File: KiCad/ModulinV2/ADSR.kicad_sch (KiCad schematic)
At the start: 54 parts, among them IC34 AS3310D, IC35 AS3310D

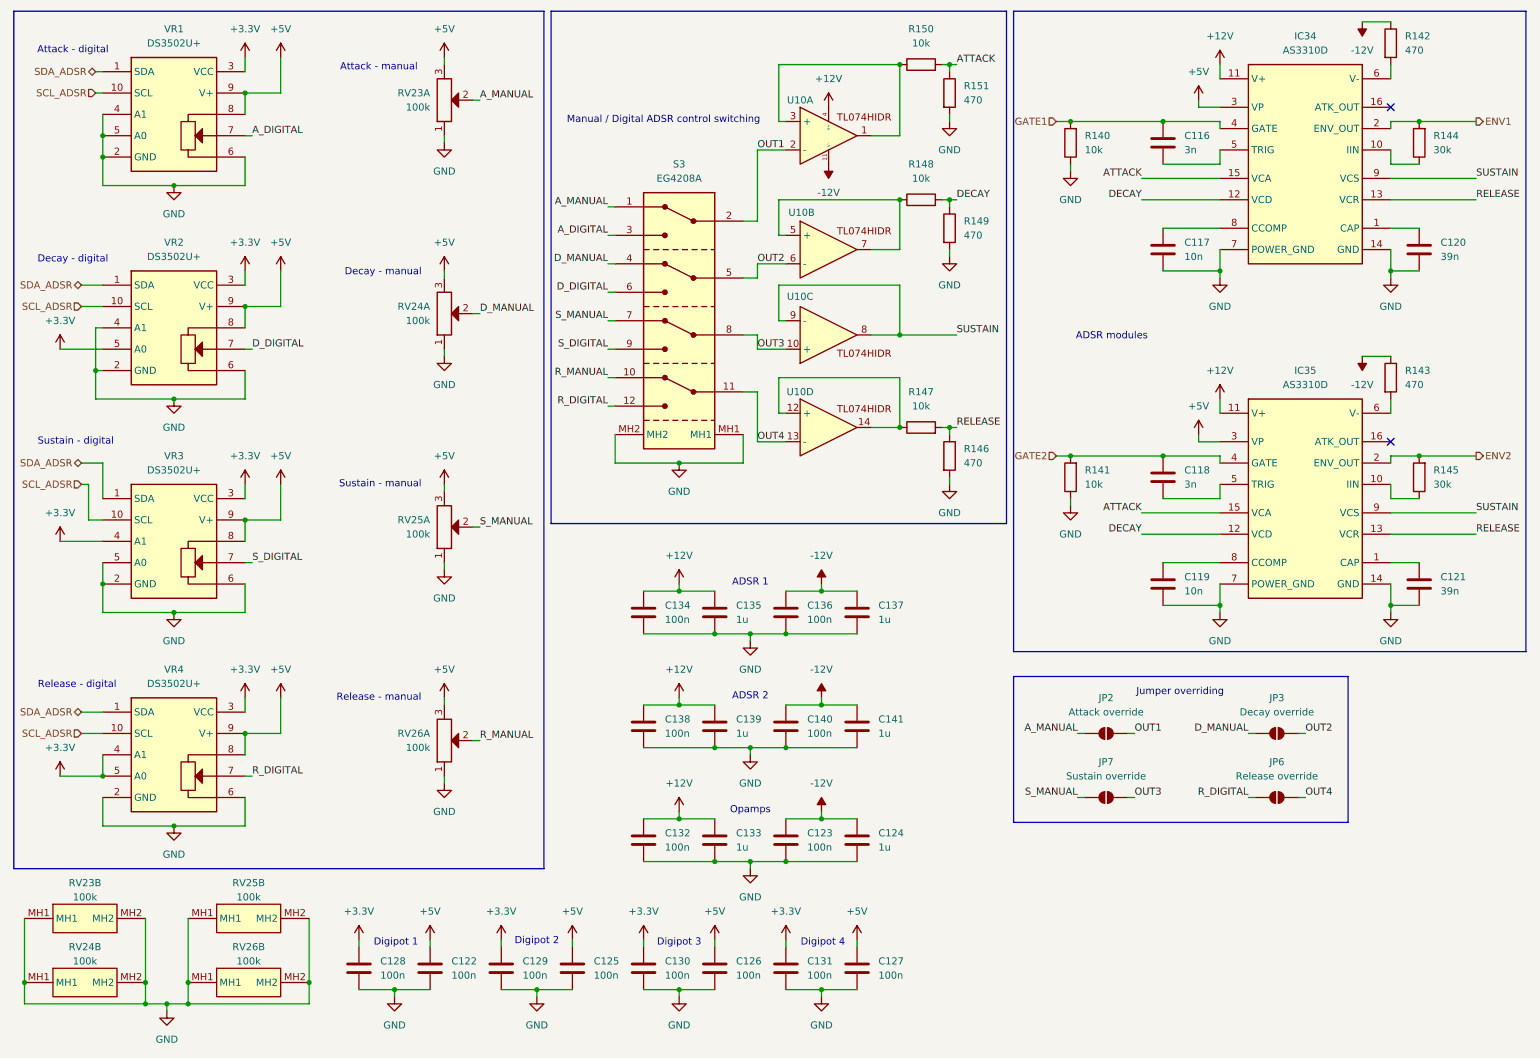
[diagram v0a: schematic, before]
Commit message: Added 4k7 pullups to I2C lines
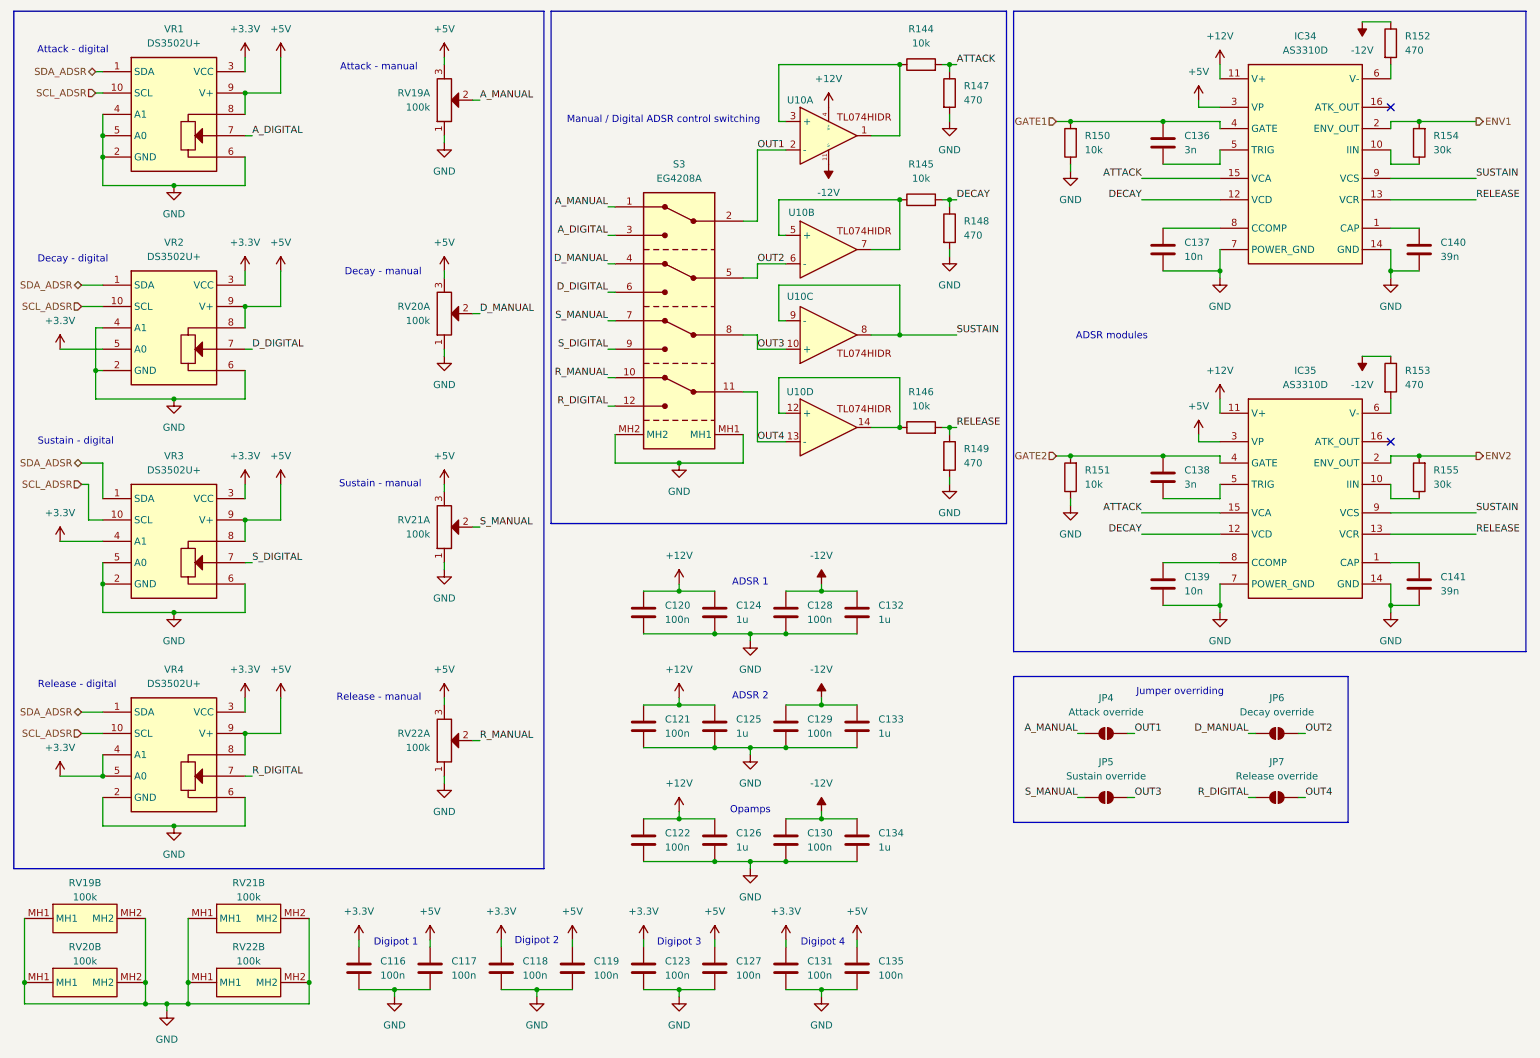
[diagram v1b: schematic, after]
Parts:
- renumbered C128 to C116, C122 to C117, C129 to C118, C125 to C119, C134 to C120, C138 to C121, C132 to C122, C130 to C123, C135 to C124, C139 to C125, C133 to C126, C126 to C127, C136 to C128, C140 to C129, C123 to C130, C137 to C132, C141 to C133, C124 to C134, C127 to C135, C116 to C136, C117 to C137, C118 to C138, C119 to C139, C120 to C140, C121 to C141, JP2 to JP4, JP7 to JP5, JP3 to JP6, JP6 to JP7, R150 to R144, R148 to R145, R147 to R146, R151 to R147, R149 to R148, R146 to R149, R140 to R150, R141 to R151, R142 to R152, R143 to R153, R144 to R154, R145 to R155, RV23 to RV19, RV24 to RV20, RV25 to RV21, RV26 to RV22

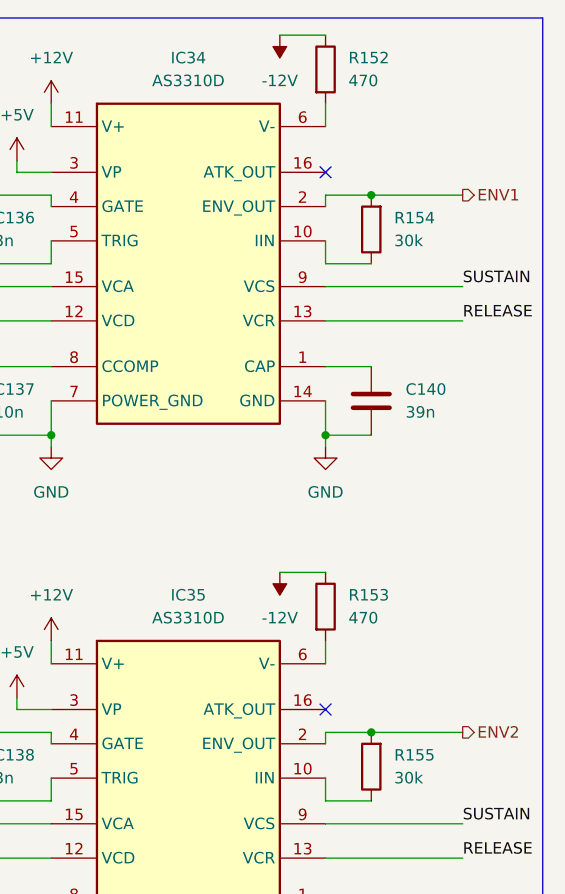
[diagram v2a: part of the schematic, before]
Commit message: Added wave selection jumpers for testing
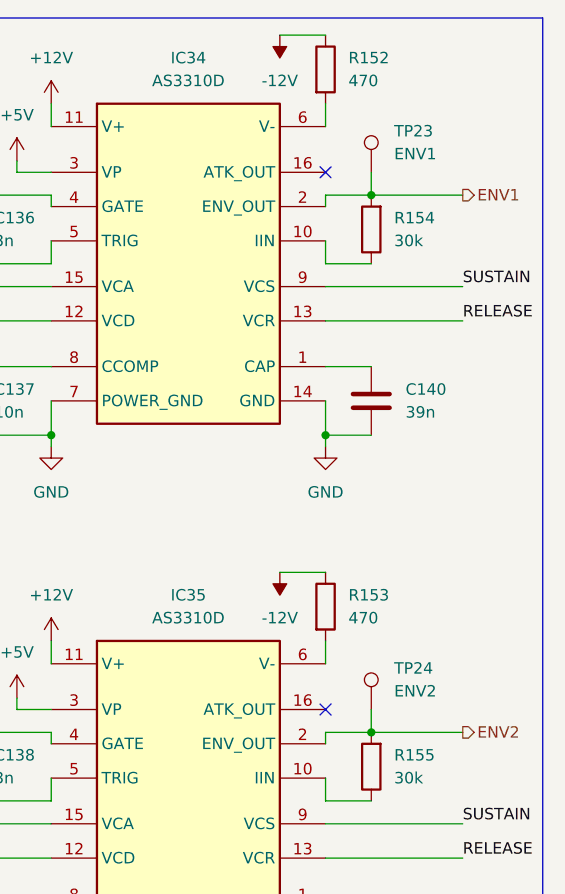
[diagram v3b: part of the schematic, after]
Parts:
- added TP23: ENV1, symbol Connector:TestPoint
- added TP24: ENV2, symbol Connector:TestPoint
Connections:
- net ENV1: now also TP23.1
- net ENV2: now also TP24.1
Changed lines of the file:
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@@
 	(wire
 		(pts
+			(xy 264.16 90.17) (xy 264.16 92.71)
+		)
+		(stroke
+			(width 0)
+			(type default)
+		)
+	)
+	(wire
+		(pts
 			(xy 224.79 29.21) (xy 224.79 30.48)
 		)
@@
 	(wire
 		(pts
+			(xy 264.16 30.48) (xy 264.16 33.02)
+		)
+		(stroke
+			(width 0)
+			(type default)
+		)
+	)
+	(wire
+		(pts
 			(xy 21.59 107.95) (xy 29.21 107.95)
 		)
@@
 	)
 	(symbol
+		(lib_id "Connector:TestPoint")
+		(at 264.16 90.17 0)
+		(unit 1)
+		(exclude_from_sim no)
+		(in_bom yes)
+		(on_board yes)
+		(dnp no)
+		(fields_autoplaced yes)
+		(property "Reference" "TP24"
+			(at 266.7 85.5979 0)
+			(effects
+				(font
+					(size 1.27 1.27)
+				)
+				(justify left)
+			)
+		)
+		(property "Value" "ENV2"
+			(at 266.7 88.1379 0)
+			(effects
+				(font
+					(size 1.27 1.27)
+				)
+				(justify left)
+			)
+		)
+		(property "Footprint" ""
+			(at 269.24 90.17 0)
+			(effects
+				(font
+					(size 1.27 1.27)
+				)
+				(hide yes)
+			)
+		)
+		(property "Datasheet" "~"
+			(at 269.24 90.17 0)
+			(effects
+				(font
+					(size 1.27 1.27)
+				)
+				(hide yes)
+			)
+		)
+		(property "Description" "test point"
+			(at 264.16 90.17 0)
+			(effects
+				(font
+					(size 1.27 1.27)
+				)
+				(hide yes)
+			)
+		)
+		(pin "1"
+		)
+		(instances
+			(project "ModulinV2"
+				(path "/c6b34a57-3941-4b56-8b80-1848c7f41082/72de756e-4613-4cf7-8685-e4594fe0f098"
+					(reference "TP24")
+					(unit 1)
+				)
+			)
+		)
+	)
+	(symbol
 		(lib_id "DS3502U+:DS3502U+")
 		(at 29.21 138.43 0)
@@
 					(unit 1)
 				)
+			)
+		)
+	)
+	(symbol
+		(lib_id "Connector:TestPoint")
+		(at 264.16 30.48 0)
+		(unit 1)
+		(exclude_from_sim no)
+		(in_bom yes)
+		(on_board yes)
+		(dnp no)
+		(fields_autoplaced yes)
+		(property "Reference" "TP23"
+			(at 266.7 25.9079 0)
+			(effects
+				(font
+					(size 1.27 1.27)
+				)
+				(justify left)
+			)
+		)
+		(property "Value" "ENV1"
+			(at 266.7 28.4479 0)
+			(effects
+				(font
+					(size 1.27 1.27)
+				)
+				(justify left)
+			)
+		)
+		(property "Footprint" ""
+			(at 269.24 30.48 0)
+			(effects
+				(font
+					(size 1.27 1.27)
+				)
+				(hide yes)
+			)
+		)
+		(property "Datasheet" "~"
+			(at 269.24 30.48 0)
+			(effects
+				(font
+					(size 1.27 1.27)
+				)
+				(hide yes)
+			)
+		)
+		(property "Description" "test point"
+			(at 264.16 30.48 0)
+			(effects
+				(font
+					(size 1.27 1.27)
+				)
+				(hide yes)
+			)
+		)
+		(pin "1"
+		)
+		(instances
+			(project ""
+				(path "/c6b34a57-3941-4b56-8b80-1848c7f41082/72de756e-4613-4cf7-8685-e4594fe0f098"
+					(reference "TP23")
+					(unit 1)
+				)

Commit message: Revert "Modified selection LED schematic and supply caps"
This reverts commit f7ca9d31056dcb2cadf4048ae59e1f5625a2aefa.
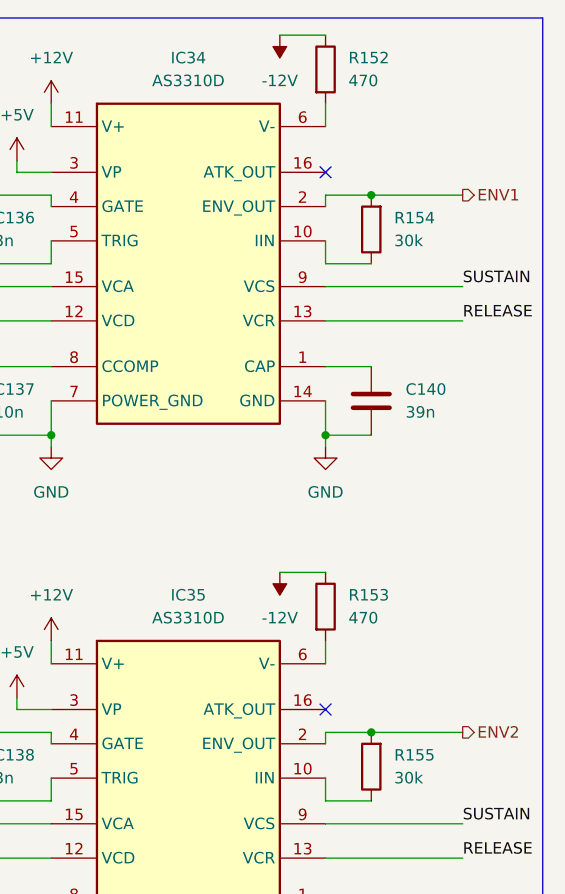
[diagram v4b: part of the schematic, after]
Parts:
- removed TP23: ENV1, symbol Connector:TestPoint
- removed TP24: ENV2, symbol Connector:TestPoint
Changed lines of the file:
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@@
 	(wire
 		(pts
-			(xy 264.16 90.17) (xy 264.16 92.71)
-		)
-		(stroke
-			(width 0)
-			(type default)
-		)
-	)
-	(wire
-		(pts
 			(xy 224.79 29.21) (xy 224.79 30.48)
 		)
@@
 	(wire
 		(pts
-			(xy 264.16 30.48) (xy 264.16 33.02)
-		)
-		(stroke
-			(width 0)
-			(type default)
-		)
-	)
-	(wire
-		(pts
 			(xy 21.59 107.95) (xy 29.21 107.95)
 		)
@@
 	)
 	(symbol
-		(lib_id "Connector:TestPoint")
-		(at 264.16 90.17 0)
-		(unit 1)
-		(exclude_from_sim no)
-		(in_bom yes)
-		(on_board yes)
-		(dnp no)
-		(fields_autoplaced yes)
-		(property "Reference" "TP24"
-			(at 266.7 85.5979 0)
-			(effects
-				(font
-					(size 1.27 1.27)
-				)
-				(justify left)
-			)
-		)
-		(property "Value" "ENV2"
-			(at 266.7 88.1379 0)
-			(effects
-				(font
-					(size 1.27 1.27)
-				)
-				(justify left)
-			)
-		)
-		(property "Footprint" ""
-			(at 269.24 90.17 0)
-			(effects
-				(font
-					(size 1.27 1.27)
-				)
-				(hide yes)
-			)
-		)
-		(property "Datasheet" "~"
-			(at 269.24 90.17 0)
-			(effects
-				(font
-					(size 1.27 1.27)
-				)
-				(hide yes)
-			)
-		)
-		(property "Description" "test point"
-			(at 264.16 90.17 0)
-			(effects
-				(font
-					(size 1.27 1.27)
-				)
-				(hide yes)
-			)
-		)
-		(pin "1"
-		)
-		(instances
-			(project "ModulinV2"
-				(path "/c6b34a57-3941-4b56-8b80-1848c7f41082/72de756e-4613-4cf7-8685-e4594fe0f098"
-					(reference "TP24")
-					(unit 1)
-				)
-			)
-		)
-	)
-	(symbol
 		(lib_id "DS3502U+:DS3502U+")
 		(at 29.21 138.43 0)
@@
 					(unit 1)
 				)
-			)
-		)
-	)
-	(symbol
-		(lib_id "Connector:TestPoint")
-		(at 264.16 30.48 0)
-		(unit 1)
-		(exclude_from_sim no)
-		(in_bom yes)
-		(on_board yes)
-		(dnp no)
-		(fields_autoplaced yes)
-		(property "Reference" "TP23"
-			(at 266.7 25.9079 0)
-			(effects
-				(font
-					(size 1.27 1.27)
-				)
-				(justify left)
-			)
-		)
-		(property "Value" "ENV1"
-			(at 266.7 28.4479 0)
-			(effects
-				(font
-					(size 1.27 1.27)
-				)
-				(justify left)
-			)
-		)
-		(property "Footprint" ""
-			(at 269.24 30.48 0)
-			(effects
-				(font
-					(size 1.27 1.27)
-				)
-				(hide yes)
-			)
-		)
-		(property "Datasheet" "~"
-			(at 269.24 30.48 0)
-			(effects
-				(font
-					(size 1.27 1.27)
-				)
-				(hide yes)
-			)
-		)
-		(property "Description" "test point"
-			(at 264.16 30.48 0)
-			(effects
-				(font
-					(size 1.27 1.27)
-				)
-				(hide yes)
-			)
-		)
-		(pin "1"
-		)
-		(instances
-			(project ""
-				(path "/c6b34a57-3941-4b56-8b80-1848c7f41082/72de756e-4613-4cf7-8685-e4594fe0f098"
-					(reference "TP23")
-					(unit 1)
-				)
